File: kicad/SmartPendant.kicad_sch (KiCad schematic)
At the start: 49 parts, among them J1 UART, J2 ST-LINK, J3 Encoder, J4 Display, J5 USB_C_Receptacle_USB2.0_16P, J6 Micro_SD_Card_Det1, Q1 MMBT3904, U1 WEACT BLACKPILL F4X1, U2 AMS1117-3.3, U3 MB85RC256VPNF-G-JNERE1

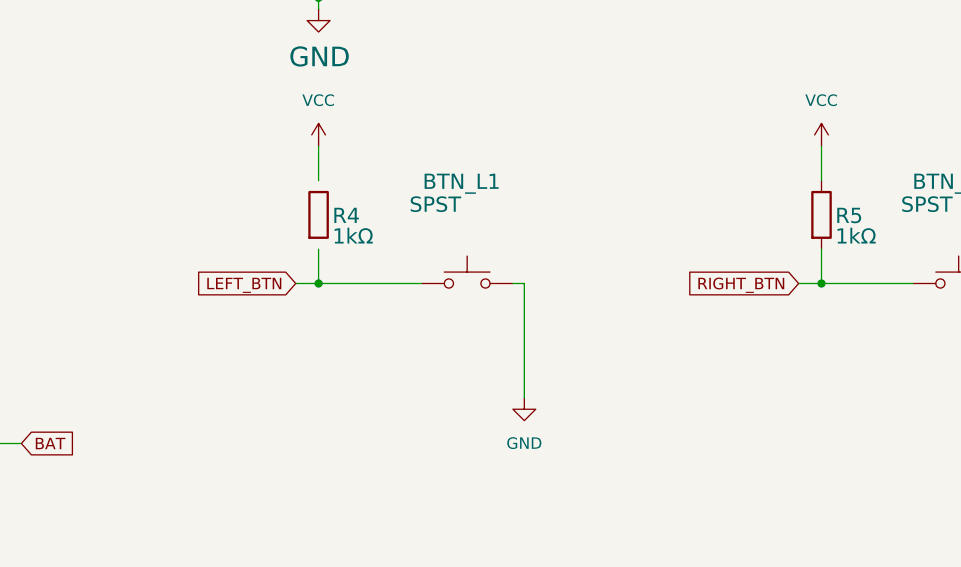
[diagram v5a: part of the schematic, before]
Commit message: Swap left and right front buttons.
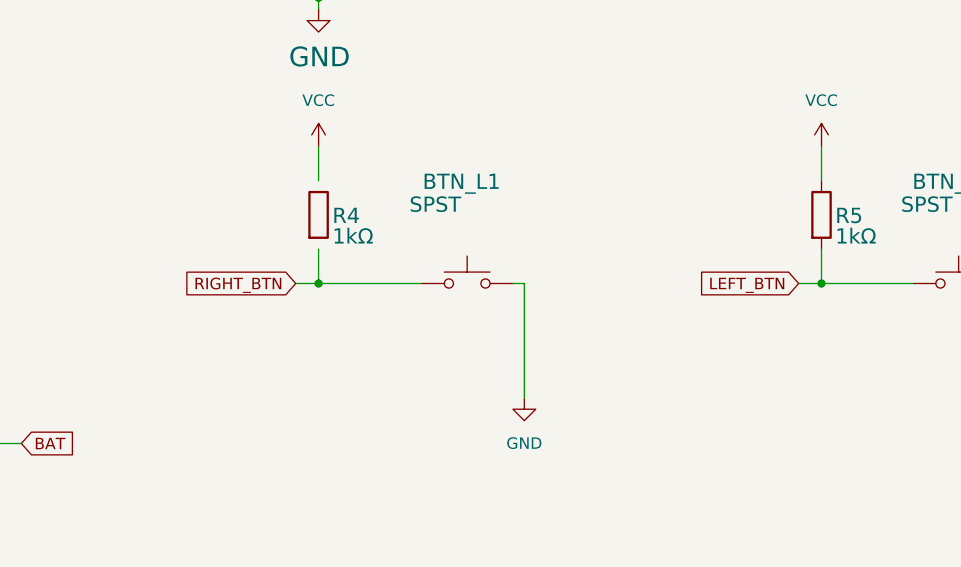
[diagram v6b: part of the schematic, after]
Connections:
- net LEFT_BTN: now also BTN_R1.1, R5.2; no longer BTN_L1.1
- net RIGHT_BTN: now also BTN_L1.1; no longer BTN_R1.1, R5.2
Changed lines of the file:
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@@
 		)
 	)
-	(global_label "LEFT_BTN"
+	(global_label "RIGHT_BTN"
 		(shape input)
 		(at 226.06 228.6 180)
@@
 		)
 	)
-	(global_label "RIGHT_BTN"
+	(global_label "LEFT_BTN"
 		(shape input)
 		(at 281.94 228.6 180)
